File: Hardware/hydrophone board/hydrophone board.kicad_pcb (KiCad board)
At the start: 2 copper layers, 6 parts, among them U1 AD8541ARTZ, U2 AD8648ARZ, U3 XLV320ADC5140IRTWR, U4 DEV-16771, U5 LT1963AxST-3.3, X1 ASE-xxxMHz

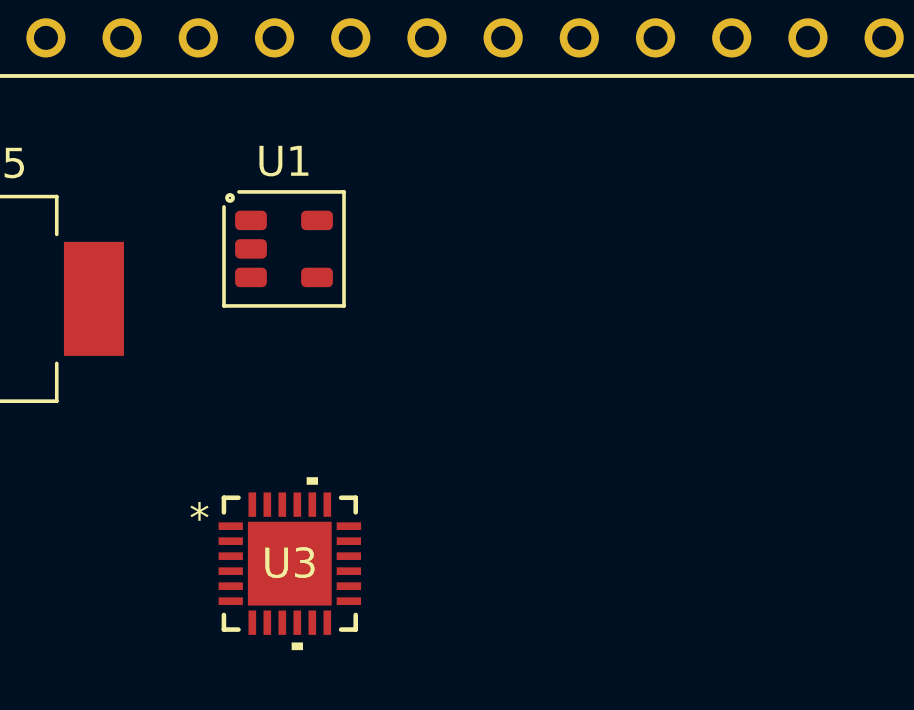
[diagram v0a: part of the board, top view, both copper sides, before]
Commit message: added teensy 3d model
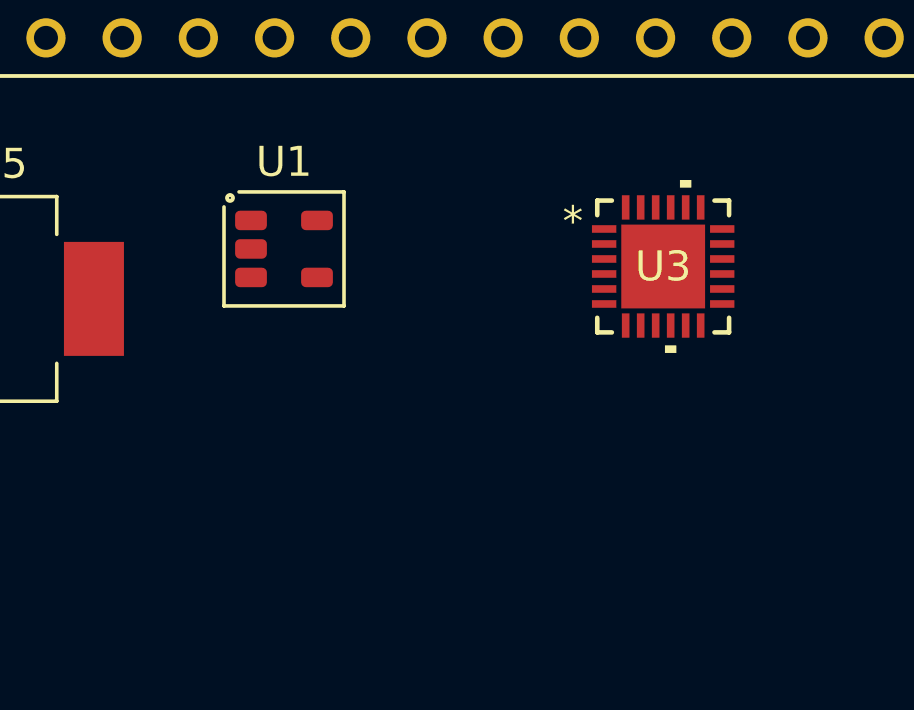
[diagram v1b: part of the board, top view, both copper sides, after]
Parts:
- moved U3 15.9 mm to (149.4, 80.5)
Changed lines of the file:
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@@
   (net 95 "Net-(X1-OUT)")
   (footprint "TLV320ADC5140:RTW24_4P15X4P15_TEX" (layer "F.Cu")
-    (at 136.906 90.424)
+    (at 149.352 80.518)
     (tags "XLV320ADC5140IRTWR ")
     (property "Sheetfile" "adc.kicad_sch")
@@
     (pad "VUSB" thru_hole circle (at -26.67 -5.08) (size 1.308 1.308) (drill 0.8) (layers "*.Cu" "*.Mask")
       (net 41 "unconnected-(U4-PadVUSB)") (pinfunction "VUSB") (pintype "passive") (solder_mask_margin 0.102))
+    (model "${KIPRJMOD}/library/teensy 4.1/footprints.pretty/DEV-16771.step"
+      (offset (xyz 0 0 0))
+      (scale (xyz 1 1 1))
+      (rotate (xyz -90 0 0))
+    )
   )
   (footprint "Package_SO_AKL:SOIC-14_3.9x8.7mm_P1.27mm" (layer "F.Cu")

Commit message: started layout
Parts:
- removed U4: DEV-16771, DEV-16771:MODULE_DEV-16771
- removed X1: ASE-xxxMHz, Oscillator:Oscillator_SMD_Abracon_ASE-4Pin_3.2x2.5mm
- added C111: 0.1u, Capacitor_SMD:C_0603_1608Metric, F.Cu at (101.6, 56.7)
- added C112: 820p, Capacitor_SMD:C_0603_1608Metric, F.Cu at (101.6, 59.2)
- added C113: 6.8u, Capacitor_SMD:C_0805_2012Metric, F.Cu at (105.8, 61.6)
- added C114: 1u, Capacitor_SMD:C_0603_1608Metric, F.Cu at (101.6, 61.7)
- added C121: 0.1u, Capacitor_SMD:C_0603_1608Metric, F.Cu at (103.1, 49.3)
- added C122: 820p, Capacitor_SMD:C_0603_1608Metric, F.Cu at (108.7, 44.7)
- added C123: 6.8u, Capacitor_SMD:C_0805_2012Metric, F.Cu at (100.3, 44.7)
- added C124: 1u, Capacitor_SMD:C_0603_1608Metric, F.Cu at (109.7, 49.3)
- added C131: 0.1u, Capacitor_SMD:C_0603_1608Metric, F.Cu at (152.0, 35.9)
- added C132: 820p, Capacitor_SMD:C_0603_1608Metric, F.Cu at (152.0, 38.4)
- added C133: 6.8u, Capacitor_SMD:C_0805_2012Metric, F.Cu at (156.2, 45.7)
- added C134: 1u, Capacitor_SMD:C_0603_1608Metric, F.Cu at (152.0, 40.9)
- added C141: 0.1u, Capacitor_SMD:C_0603_1608Metric, F.Cu at (140.9, 35.9)
- added C142: 820p, Capacitor_SMD:C_0603_1608Metric, F.Cu at (140.9, 38.4)
- added C143: 6.8u, Capacitor_SMD:C_0805_2012Metric, F.Cu at (145.1, 45.7)
- added C144: 1u, Capacitor_SMD:C_0603_1608Metric, F.Cu at (140.9, 40.9)
- added C211: 360p, Capacitor_SMD:C_0603_1608Metric, F.Cu at (149.8, 77.7)
- added C212: 360p, Capacitor_SMD:C_0603_1608Metric, F.Cu at (149.8, 80.2)
- added C213: 0.1u, Capacitor_SMD:C_0603_1608Metric, F.Cu at (149.8, 82.7)
- added C214: 360p, Capacitor_SMD:C_0603_1608Metric, F.Cu at (149.8, 85.2)
- added C215: 36p, Capacitor_SMD:C_0603_1608Metric, F.Cu at (149.8, 87.7)
- added C216: 36p, Capacitor_SMD:C_0603_1608Metric, F.Cu at (149.8, 90.2)
- added C217: 18p, Capacitor_SMD:C_0603_1608Metric, F.Cu at (153.8, 77.7)
- added C218: 360p, Capacitor_SMD:C_0603_1608Metric, F.Cu at (153.8, 80.2)
- added C221: 360p, Capacitor_SMD:C_0603_1608Metric, F.Cu at (75.7, 108.5)
- added C222: 360p, Capacitor_SMD:C_0603_1608Metric, F.Cu at (75.7, 111.0)
- added C223: 0.1u, Capacitor_SMD:C_0603_1608Metric, F.Cu at (75.7, 113.5)
- added C224: 360p, Capacitor_SMD:C_0603_1608Metric, F.Cu at (75.7, 116.0)
- added C225: 36p, Capacitor_SMD:C_0603_1608Metric, F.Cu at (75.7, 118.6)
- added C226: 36p, Capacitor_SMD:C_0603_1608Metric, F.Cu at (75.7, 121.1)
- added C227: 18p, Capacitor_SMD:C_0603_1608Metric, F.Cu at (79.7, 108.5)
- added C228: 360p, Capacitor_SMD:C_0603_1608Metric, F.Cu at (79.7, 111.0)
- added C231: 360p, Capacitor_SMD:C_0603_1608Metric, F.Cu at (98.4, 108.5)
- added C232: 360p, Capacitor_SMD:C_0603_1608Metric, F.Cu at (98.4, 111.0)
- added C233: 0.1u, Capacitor_SMD:C_0603_1608Metric, F.Cu at (98.4, 113.5)
- added C234: 360p, Capacitor_SMD:C_0603_1608Metric, F.Cu at (98.4, 116.0)
- added C235: 36p, Capacitor_SMD:C_0603_1608Metric, F.Cu at (98.4, 118.6)
- added C236: 36p, Capacitor_SMD:C_0603_1608Metric, F.Cu at (98.4, 121.1)
- added C237: 18p, Capacitor_SMD:C_0603_1608Metric, F.Cu at (102.4, 108.5)
- added C238: 360p, Capacitor_SMD:C_0603_1608Metric, F.Cu at (102.4, 111.0)
- added C241: 360p, Capacitor_SMD:C_0603_1608Metric, F.Cu at (126.7, 102.1)
- added C242: 360p, Capacitor_SMD:C_0603_1608Metric, F.Cu at (126.7, 104.6)
- added C243: 0.1u, Capacitor_SMD:C_0603_1608Metric, F.Cu at (126.7, 107.1)
- added C244: 360p, Capacitor_SMD:C_0603_1608Metric, F.Cu at (126.7, 109.6)
- added C245: 36p, Capacitor_SMD:C_0603_1608Metric, F.Cu at (126.7, 112.1)
- added C246: 36p, Capacitor_SMD:C_0603_1608Metric, F.Cu at (126.7, 114.6)
- added C247: 18p, Capacitor_SMD:C_0603_1608Metric, F.Cu at (130.7, 102.1)
- added C248: 360p, Capacitor_SMD:C_0603_1608Metric, F.Cu at (130.7, 104.6)
- added C301: 0.1u, Capacitor_SMD:C_0603_1608Metric, F.Cu at (131.3, 77.7)
- added C302: 1u, Capacitor_SMD:C_0603_1608Metric, F.Cu at (131.3, 80.2)
- added C303: 0.1u, Capacitor_SMD:C_0603_1608Metric, F.Cu at (131.3, 82.7)
- added C304: 10u, Capacitor_SMD:C_0805_2012Metric, F.Cu at (143.5, 77.9)
- added C305: 1u, Capacitor_SMD:C_0603_1608Metric, F.Cu at (131.3, 85.2)
- added C306: 0.1u, Capacitor_SMD:C_0603_1608Metric, F.Cu at (131.3, 87.7)
- added C307: 10u, Capacitor_SMD:C_0805_2012Metric, F.Cu at (143.5, 80.9)
- added C308: 1u, Capacitor_SMD:C_0603_1608Metric, F.Cu at (131.3, 90.2)
- added C309: 0.1u, Capacitor_SMD:C_0603_1608Metric, F.Cu at (131.3, 92.7)
- added C310: 1u, Capacitor_SMD:C_0603_1608Metric, F.Cu at (135.3, 77.7)
- added C311: 1u, Capacitor_SMD:C_0603_1608Metric, F.Cu at (135.3, 80.2)
- added C312: 1u, Capacitor_SMD:C_0603_1608Metric, F.Cu at (135.3, 82.7)
- added C313: 1u, Capacitor_SMD:C_0603_1608Metric, F.Cu at (135.3, 85.2)
- added C314: 1u, Capacitor_SMD:C_0603_1608Metric, F.Cu at (135.3, 87.7)
- added C315: 1u, Capacitor_SMD:C_0603_1608Metric, F.Cu at (135.3, 90.2)
- added C316: 1u, Capacitor_SMD:C_0603_1608Metric, F.Cu at (135.3, 92.7)
- added C317: 1u, Capacitor_SMD:C_0603_1608Metric, F.Cu at (139.3, 77.7)
- added C318: 1u, Capacitor_SMD:C_0603_1608Metric, F.Cu at (139.3, 80.2)
- added C501: 1u, Capacitor_SMD:C_0603_1608Metric, F.Cu at (154.1, 102.1)
- added C502: 22u, Capacitor_SMD:C_0805_2012Metric, F.Cu at (162.9, 102.3)
- added C503: 22u, Capacitor_SMD:C_0805_2012Metric, F.Cu at (162.9, 105.3)
- added C504: 1u, Capacitor_SMD:C_0603_1608Metric, F.Cu at (154.1, 104.6)
- added C505: 22u, Capacitor_SMD:C_0805_2012Metric, F.Cu at (162.9, 108.3)
- added C506: 1u, Capacitor_SMD:C_0603_1608Metric, F.Cu at (154.1, 107.1)
- added D501: LED, LED_SMD:LED_0805_2012Metric, F.Cu at (158.3, 112.0)
- added D502: LED, LED_SMD:LED_0805_2012Metric, F.Cu at (158.3, 115.1)
- added J1: AudioJack3_Ground, Connector_Audio:Jack_3.5mm_CUI_SJ-3524-SMT_Horizontal, F.Cu at (72.4, 44.5)
- added J2: AudioJack3_Ground, Connector_Audio:Jack_3.5mm_CUI_SJ-3524-SMT_Horizontal, F.Cu at (72.4, 59.7)
- added J3: AudioJack3_Ground, Connector_Audio:Jack_3.5mm_CUI_SJ-3524-SMT_Horizontal, F.Cu at (72.4, 73.7)
- added J301: Conn_01x08, Connector_PinSocket_2.54mm:PinSocket_1x08_P2.54mm_Vertical, F.Cu at (127.0, 78.7)
- added J4: AudioJack3_Ground, Connector_Audio:Jack_3.5mm_CUI_SJ-3524-SMT_Horizontal, F.Cu at (72.4, 88.9)
- added J401: Conn_01x07, Connector_PinHeader_2.54mm:PinHeader_1x07_P2.54mm_Vertical, F.Cu at (219.7, 50.8)
- added J5: Conn_01x02, Connector_PinHeader_2.54mm:PinHeader_1x02_P2.54mm_Vertical, F.Cu at (76.0, 100.4)
- added J501: Conn_01x03, Connector_PinSocket_2.54mm:PinSocket_1x03_P2.54mm_Vertical, F.Cu at (158.4, 103.1)
- added J6: Conn_01x02, Connector_PinHeader_2.54mm:PinHeader_1x02_P2.54mm_Vertical, F.Cu at (80.7, 100.4)
- added J7: Conn_01x02, Connector_PinHeader_2.54mm:PinHeader_1x02_P2.54mm_Vertical, F.Cu at (85.3, 100.4)
- added J8: Conn_01x02, Connector_PinHeader_2.54mm:PinHeader_1x02_P2.54mm_Vertical, F.Cu at (90.0, 100.4)
- added L501: L_Ferrite_Small, Inductor_SMD:L_0805_2012Metric, F.Cu at (162.8, 111.9)
- added R111: 715, Resistor_SMD:R_0603_1608Metric, F.Cu at (101.6, 64.2)
- added R112: 360, Resistor_SMD:R_0603_1608Metric, F.Cu at (101.6, 66.7)
- added R113: 10k, Resistor_SMD:R_0603_1608Metric, F.Cu at (101.6, 69.3)
- added R114: 10k, Resistor_SMD:R_0603_1608Metric, F.Cu at (101.6, 71.8)
- added R121: 715, Resistor_SMD:R_0603_1608Metric, F.Cu at (111.3, 44.7)
- added R122: 360, Resistor_SMD:R_0603_1608Metric, F.Cu at (100.3, 49.3)
- added R123: 10k, Resistor_SMD:R_0603_1608Metric, F.Cu at (106.4, 48.5)
- added R124: 10k, Resistor_SMD:R_0603_1608Metric, F.Cu at (112.3, 49.3)
- added R131: 715, Resistor_SMD:R_0603_1608Metric, F.Cu at (152.0, 43.4)
- added R132: 360, Resistor_SMD:R_0603_1608Metric, F.Cu at (152.0, 46.0)
- added R133: 10k, Resistor_SMD:R_0603_1608Metric, F.Cu at (152.0, 48.5)
- added R134: 10k, Resistor_SMD:R_0603_1608Metric, F.Cu at (152.0, 51.0)
- added R141: 715, Resistor_SMD:R_0603_1608Metric, F.Cu at (140.9, 43.4)
- added R142: 360, Resistor_SMD:R_0603_1608Metric, F.Cu at (140.9, 46.0)
- added R143: 10k, Resistor_SMD:R_0603_1608Metric, F.Cu at (140.9, 48.5)
- added R144: 10k, Resistor_SMD:R_0603_1608Metric, F.Cu at (140.9, 51.0)
- added R211: 5.62k, Resistor_SMD:R_0603_1608Metric, F.Cu at (153.8, 82.7)
- added R212: 169k, Resistor_SMD:R_0603_1608Metric, F.Cu at (153.8, 85.2)
- added R213: 8.45k, Resistor_SMD:R_0603_1608Metric, F.Cu at (153.8, 87.7)
- added R214: 115k, Resistor_SMD:R_0603_1608Metric, F.Cu at (153.8, 90.2)
- added R215: 44.2k, Resistor_SMD:R_0603_1608Metric, F.Cu at (157.8, 77.7)
- added R216: 44.2k, Resistor_SMD:R_0603_1608Metric, F.Cu at (157.8, 80.2)
- added R217: 9.76k, Resistor_SMD:R_0603_1608Metric, F.Cu at (157.8, 82.7)
- added R221: 5.62k, Resistor_SMD:R_0603_1608Metric, F.Cu at (79.7, 113.5)
- added R222: 169k, Resistor_SMD:R_0603_1608Metric, F.Cu at (79.7, 116.0)
- added R223: 8.45k, Resistor_SMD:R_0603_1608Metric, F.Cu at (79.7, 118.6)
- added R224: 115k, Resistor_SMD:R_0603_1608Metric, F.Cu at (79.7, 121.1)
- added R225: 44.2k, Resistor_SMD:R_0603_1608Metric, F.Cu at (83.7, 108.5)
- added R226: 44.2k, Resistor_SMD:R_0603_1608Metric, F.Cu at (83.7, 111.0)
- added R227: 9.76k, Resistor_SMD:R_0603_1608Metric, F.Cu at (83.7, 113.5)
- added R231: 5.62k, Resistor_SMD:R_0603_1608Metric, F.Cu at (102.4, 113.5)
- added R232: 169k, Resistor_SMD:R_0603_1608Metric, F.Cu at (102.4, 116.0)
- added R233: 8.45k, Resistor_SMD:R_0603_1608Metric, F.Cu at (102.4, 118.6)
- added R234: 115k, Resistor_SMD:R_0603_1608Metric, F.Cu at (102.4, 121.1)
- added R235: 44.2k, Resistor_SMD:R_0603_1608Metric, F.Cu at (106.5, 108.5)
- added R236: 44.2k, Resistor_SMD:R_0603_1608Metric, F.Cu at (106.5, 111.0)
- added R237: 9.76k, Resistor_SMD:R_0603_1608Metric, F.Cu at (106.5, 113.5)
- added R241: 5.62k, Resistor_SMD:R_0603_1608Metric, F.Cu at (130.7, 107.1)
- added R242: 169k, Resistor_SMD:R_0603_1608Metric, F.Cu at (130.7, 109.6)
- added R243: 8.45k, Resistor_SMD:R_0603_1608Metric, F.Cu at (130.7, 112.1)
- added R244: 115k, Resistor_SMD:R_0603_1608Metric, F.Cu at (130.7, 114.6)
- added R245: 44.2k, Resistor_SMD:R_0603_1608Metric, F.Cu at (134.7, 102.1)
- added R246: 44.2k, Resistor_SMD:R_0603_1608Metric, F.Cu at (134.7, 104.6)
- added R247: 9.76k, Resistor_SMD:R_0603_1608Metric, F.Cu at (134.7, 107.1)
- added R301: 2k, Resistor_SMD:R_0603_1608Metric, F.Cu at (139.3, 82.7)
- added R302: 2k, Resistor_SMD:R_0603_1608Metric, F.Cu at (139.3, 85.2)
- added R303: 1k, Resistor_SMD:R_0603_1608Metric, F.Cu at (139.3, 87.7)
- added R304: 1k, Resistor_SMD:R_0603_1608Metric, F.Cu at (139.3, 90.2)
- added R305: 1k, Resistor_SMD:R_0603_1608Metric, F.Cu at (139.3, 92.7)
- added R501: 470, Resistor_SMD:R_0603_1608Metric, F.Cu at (154.1, 109.6)
- added R502: 470, Resistor_SMD:R_0603_1608Metric, F.Cu at (154.1, 112.1)
- added TP111: TestPoint_Probe, Connector_PinHeader_2.54mm:PinHeader_1x01_P2.54mm_Vertical, F.Cu at (105.9, 57.8)
- added TP121: TestPoint_Probe, Connector_PinHeader_2.54mm:PinHeader_1x01_P2.54mm_Vertical, F.Cu at (118.1, 44.5)
- added TP131: TestPoint_Probe, Connector_PinHeader_2.54mm:PinHeader_1x01_P2.54mm_Vertical, F.Cu at (156.3, 41.9)
- added TP141: TestPoint_Probe, Connector_PinHeader_2.54mm:PinHeader_1x01_P2.54mm_Vertical, F.Cu at (145.2, 41.9)
- added TP211: TestPoint_Probe, Connector_PinHeader_2.54mm:PinHeader_1x01_P2.54mm_Vertical, F.Cu at (162.1, 78.7)
- added TP221: TestPoint_Probe, Connector_PinHeader_2.54mm:PinHeader_1x01_P2.54mm_Vertical, F.Cu at (88.0, 119.9)
- added TP231: TestPoint_Probe, Connector_PinHeader_2.54mm:PinHeader_1x01_P2.54mm_Vertical, F.Cu at (110.8, 119.9)
- added TP241: TestPoint_Probe, Connector_PinHeader_2.54mm:PinHeader_1x01_P2.54mm_Vertical, F.Cu at (139.0, 113.5)
- added TP501: TestPoint_Probe, Connector_PinHeader_2.54mm:PinHeader_1x01_P2.54mm_Vertical, F.Cu at (149.8, 103.1)
- added TP502: TestPoint_Probe, Connector_PinHeader_2.54mm:PinHeader_1x01_P2.54mm_Vertical, F.Cu at (149.8, 107.8)
- added TP503: TestPoint_Probe, Connector_PinHeader_2.54mm:PinHeader_1x01_P2.54mm_Vertical, F.Cu at (149.8, 112.4)
- added TP504: TestPoint_Probe, Connector_PinHeader_2.54mm:PinHeader_1x01_P2.54mm_Vertical, F.Cu at (149.8, 117.1)
- added U121: AD8541ARTZ, Package_TO_SOT_SMD_AKL:SOT-23-5, F.Cu at (104.6, 44.7)
- added U131: AD8541ARTZ, Package_TO_SOT_SMD_AKL:SOT-23-5, F.Cu at (156.6, 37.1)
- added U141: AD8541ARTZ, Package_TO_SOT_SMD_AKL:SOT-23-5, F.Cu at (145.5, 37.1)
- added U221: AD8648ARZ, Package_SO_AKL:SOIC-14_3.9x8.7mm_P1.27mm, F.Cu at (90.1, 112.4)
- added U231: AD8648ARZ, Package_SO_AKL:SOIC-14_3.9x8.7mm_P1.27mm, F.Cu at (112.8, 112.4)
- added U241: AD8648ARZ, Package_SO_AKL:SOIC-14_3.9x8.7mm_P1.27mm, F.Cu at (141.1, 106.0)
- added U401: DEV-16771, DEV-16771:MODULE_DEV-16771, F.Cu at (203.2, 68.6)
- moved U211 82.1 mm to (190.1, 117.8)
- moved U301 82.1 mm to (223.5, 115.7)
- moved U501 82.1 mm to (201.4, 116.8)
- moved U111 33.1 mm to (106.4, 66.5)
- renumbered U1 to U111, U2 to U211, U3 to U301, U5 to U501
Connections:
- net /adc/IN_1_B renamed /IN_1_B
- U111 pad 1: /low pass filter/IN -> /IN_1_A
- U301 pad 13: unconnected-(U3-IN4M_GPO4-Pad13) -> /adc/IN4M
- U301 pad 20: /adc/MCLK -> /adc/SDOUT_2
- U501 pad 3: +3.3VA -> Net-(J501-Pin_1)
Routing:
- net Net-(U121-+): track 0.00 -> 12.7 mm
- net Net-(U121--): track 0.00 -> 11.2 mm
- net GND: track 0.00 -> 7.48 mm, vias 0 -> 3
- net /IN_2_A: track 0.00 -> 5.34 mm
- net +3.3VA: track 0.00 -> 5.25 mm
- net /IN_2: track 0.00 -> 2.54 mm

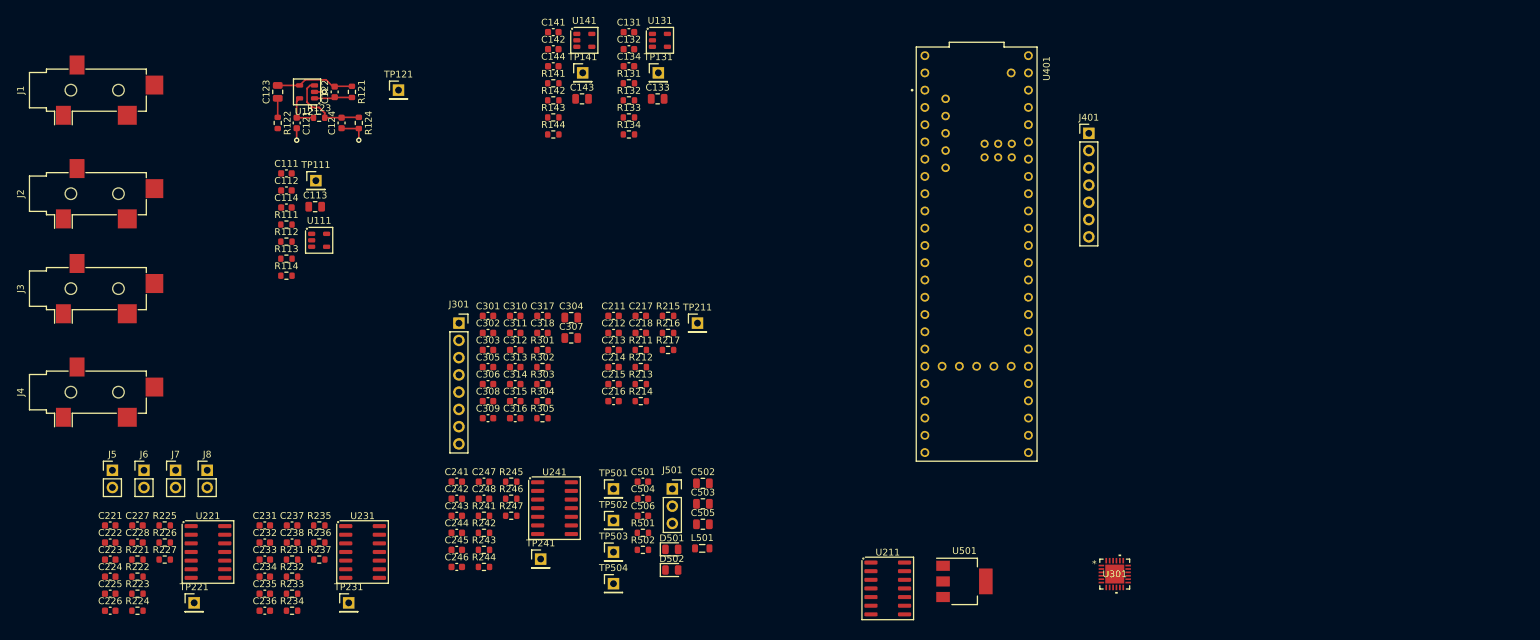
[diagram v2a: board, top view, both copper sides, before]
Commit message: changed all cap + resistors to 0805, starting filter layout
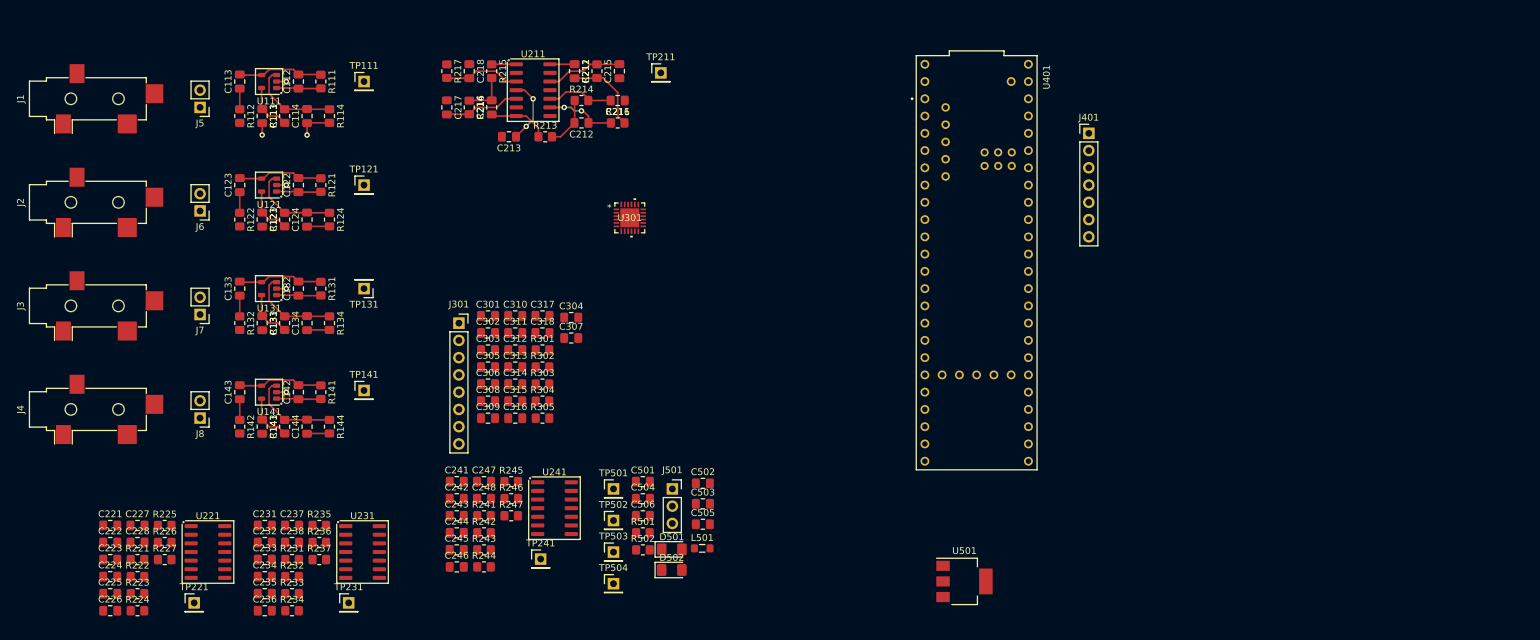
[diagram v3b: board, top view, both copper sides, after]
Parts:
- C111, C112, C114, C121, C122, C124, C131, C132, C134, C141, C142, C144, C211, C212, C213, C214, C215, C216, C217, C218, C221, C222, C223, C224, C225, C226, C227, C228, C231, C232, C233, C234, C235, C236, C237, C238, C241, C242, C243, C244, C245, C246, C247, C248, C301, C302, C303, C305, C306, C308, C309, C310, C311, C312, C313, C314, C315, C316, C317, C318, C501, C504, C506: footprint Capacitor_SMD:C_0603_1608Metric -> Capacitor_SMD:C_0805_2012Metric_Pad1.18x1.45mm_HandSolder
- C113, C123, C133, C143, C304, C307, C502, C503, C505: footprint Capacitor_SMD:C_0805_2012Metric -> Capacitor_SMD:C_0805_2012Metric_Pad1.18x1.45mm_HandSolder
- D501, D502: footprint LED_SMD:LED_0805_2012Metric -> LED_SMD:LED_1206_3216Metric_Pad1.42x1.75mm_HandSolder
- L501: footprint Inductor_SMD:L_0805_2012Metric -> Inductor_SMD:L_0805_2012Metric_Pad1.05x1.20mm_HandSolder
- R111, R112, R113, R114, R121, R122, R123, R124, R131, R132, R133, R134, R141, R142, R143, R144, R211, R212, R213, R214, R215, R216, R217, R221, R222, R223, R224, R225, R226, R227, R231, R232, R233, R234, R235, R236, R237, R241, R242, R243, R244, R245, R246, R247, R301, R302, R303, R304, R305, R501, R502: footprint Resistor_SMD:R_0603_1608Metric -> Resistor_SMD:R_0805_2012Metric_Pad1.20x1.40mm_HandSolder
- moved U211 90.0 mm to (137.9, 44.5)
- moved U301 88.6 mm to (152.1, 63.2)
- moved C141 72.2 mm to (98.0, 94.0), turned to -90 degrees
- moved U141 69.5 mm to (99.1, 88.9), turned to 180 degrees
- moved C131 68.9 mm to (98.0, 78.7), turned to -90 degrees
- moved U131 68.2 mm to (99.1, 73.7), turned to 180 degrees
- moved C133 67.6 mm to (94.7, 73.7), turned to 90 degrees
- moved R142 66.6 mm to (94.7, 94.0), turned to -90 degrees
- moved C143 66.3 mm to (94.7, 88.9), turned to 90 degrees
- moved R132 66.0 mm to (94.7, 78.7), turned to -90 degrees
- moved C144 64.2 mm to (104.6, 94.0), turned to 90 degrees
- moved C142 62.9 mm to (103.4, 88.9), turned to 90 degrees
- moved C134 60.6 mm to (104.6, 78.7), turned to 90 degrees
- moved R143 60.3 mm to (101.3, 94.0), turned to 90 degrees
- moved C132 60.1 mm to (103.4, 73.7), turned to 90 degrees
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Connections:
- J5 pad 1: /IN_1 -> GND
- J5 pad 2: GND -> /IN_1
- J6 pad 1: /IN_2 -> GND
- J6 pad 2: GND -> /IN_2
- J7 pad 1: /IN_3 -> GND
- J7 pad 2: GND -> /IN_3
- J8 pad 1: /IN_4 -> GND
- J8 pad 2: GND -> /IN_4
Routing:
- net +3.3VA: track 5.25 -> 38.7 mm, vias 0 -> 2
- net GND: track 7.48 -> 22.5 mm, vias 3 -> 6
- net Net-(U141-+): track 0.00 -> 13.4 mm
- net Net-(U111-+): track 0.00 -> 13.4 mm
- net Net-(U131-+): track 0.00 -> 13.4 mm
- net Net-(U141--): track 0.00 -> 12.6 mm
- net Net-(U111--): track 0.00 -> 12.6 mm
- net Net-(U131--): track 0.00 -> 12.6 mm
- net Net-(C211-Pad2): track 0.00 -> 12.1 mm
- net Net-(U211A-+): track 0.00 -> 11.3 mm
- net Net-(U211D-+): track 0.00 -> 11.3 mm
- net Net-(U211B-+): track 0.00 -> 11.2 mm
- net Net-(U211C--): track 0.00 -> 10.5 mm, vias 0 -> 2
- net Net-(U211C-+): track 0.00 -> 10.0 mm
- net Net-(U211B--): track 0.00 -> 8.97 mm
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
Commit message: Update hydrophone board.kicad_pcb
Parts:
- J301: footprint Connector_PinSocket_2.54mm:PinSocket_1x08_P2.54mm_Vertical -> Connector_PinHeader_2.54mm:PinHeader_1x08_P2.54mm_Vertical
- J501: footprint Connector_PinSocket_2.54mm:PinSocket_1x03_P2.54mm_Vertical -> Connector_PinHeader_2.54mm:PinHeader_1x03_P2.54mm_Vertical
- moved J301 155.0 mm to (282.0, 79.8)
- moved C225 91.6 mm to (144.8, 58.4), turned to 90 degrees
- moved C226 90.4 mm to (144.5, 62.5), turned to 180 degrees
- moved TP221 88.1 mm to (151.1, 58.4)
- moved R222 84.5 mm to (141.5, 58.4), turned to 90 degrees
- moved R224 83.5 mm to (139.2, 62.5)
- moved R221 80.5 mm to (144.5, 65.8)
- moved C221 80.1 mm to (138.2, 58.4), turned to -90 degrees
- moved C222 78.0 mm to (139.2, 65.8), turned to 180 degrees
- moved R223 74.2 mm to (133.9, 67.8)
- moved C224 72.7 mm to (126.0, 63.5), turned to 90 degrees
- moved C223 69.9 mm to (128.5, 67.8), turned to 180 degrees
- moved C228 67.9 mm to (122.7, 58.4), turned to -90 degrees
- moved U221 66.4 mm to (132.1, 61.0)
- moved R227 65.7 mm to (119.4, 58.4), turned to -90 degrees
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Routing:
- net GND: track 22.5 -> 150.7 mm, vias 6 -> 43
- net +3.3VA: track 38.7 -> 96.0 mm, vias 2 -> 8
- net /IN_4: track 3.04 -> 32.2 mm
- net /IN_3: track 3.04 -> 32.2 mm
- net /IN_1: track 3.04 -> 32.2 mm
- net /IN_2: track 3.04 -> 32.2 mm
- net +3.3VD: track 0.00 -> 28.2 mm, vias 0 -> 2
- net Net-(U231C--): track 0.00 -> 14.9 mm, vias 0 -> 2
- net Net-(U241C--): track 0.00 -> 14.9 mm, vias 0 -> 2
- net Net-(U221C--): track 0.00 -> 14.9 mm, vias 0 -> 2
- net Net-(U301-VREF): track 0.00 -> 14.7 mm
- net /IN_4_A: track 6.57 -> 20.2 mm
- net /IN_2_A: track 6.57 -> 20.2 mm
- net /IN_1_A: track 6.57 -> 20.2 mm
- net /IN_3_A: track 6.52 -> 20.2 mm
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
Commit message: changed some aprts
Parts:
- removed J301: Conn_01x08, Connector_PinHeader_2.54mm:PinHeader_1x08_P2.54mm_Vertical
- removed J501: Conn_01x03, Connector_PinHeader_2.54mm:PinHeader_1x03_P2.54mm_Vertical
- removed TP111, TP121, TP131, TP141, TP211, TP221, TP231, TP241: TestPoint_Probe, Connector_PinHeader_2.54mm:PinHeader_1x01_P2.54mm_Vertical
- added J111: Conn_01x02, Connector_PinHeader_2.54mm:PinHeader_1x02_P2.54mm_Vertical, F.Cu at (124.4, 119.4)
- added J121: Conn_01x02, Connector_PinHeader_2.54mm:PinHeader_1x02_P2.54mm_Vertical, F.Cu at (131.1, 119.4)
- added J131: Conn_01x02, Connector_PinHeader_2.54mm:PinHeader_1x02_P2.54mm_Vertical, F.Cu at (131.1, 110.2)
- added J141: Conn_01x02, Connector_PinHeader_2.54mm:PinHeader_1x02_P2.54mm_Vertical, F.Cu at (111.1, 119.4)
- added J211: Conn_01x02, Connector_PinHeader_2.54mm:PinHeader_1x02_P2.54mm_Vertical, F.Cu at (124.4, 110.2)
- added J221: Conn_01x02, Connector_PinHeader_2.54mm:PinHeader_1x02_P2.54mm_Vertical, F.Cu at (117.8, 110.2)
- added J231: Conn_01x02, Connector_PinHeader_2.54mm:PinHeader_1x02_P2.54mm_Vertical, F.Cu at (117.8, 119.4)
- added J241: Conn_01x02, Connector_PinHeader_2.54mm:PinHeader_1x02_P2.54mm_Vertical, F.Cu at (111.1, 110.2)
- added JP501: Jumper_3_Bridged12, PCM_4ms_SolderJumper:JUMPER_SMD_1x3, F.Cu at (167.9, 87.9)
- moved TP501 85.4 mm to (210.8, 43.4)
- moved J401 35.0 mm to (212.3, 78.7), turned to 180 degrees
- moved TP504 29.7 mm to (156.5, 88.1)
- moved R501 28.0 mm to (179.3, 89.2), turned to 180 degrees
- moved TP503 24.5 mm to (152.7, 88.1)
- moved U401 23.0 mm to (195.6, 68.6)
- moved TP502 22.3 mm to (160.3, 88.1)
- moved U501 19.1 mm to (171.7, 94.7)
- moved C505 18.6 mm to (156.0, 97.0)
- moved C501 18.6 mm to (181.1, 97.0)
- moved C502 18.6 mm to (177.8, 97.0)
- moved C503 18.6 mm to (165.9, 97.0)
- moved C504 18.6 mm to (162.6, 97.0)
- moved C506 18.6 mm to (152.7, 97.0)
- moved D501 18.6 mm to (179.3, 92.5)
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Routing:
- net +3.3VD: track 28.2 -> 39.3 mm
- net +3.3VA: track 96.0 -> 103.3 mm
- net GND: track 150.7 -> 156.1 mm, vias 43 -> 47
- net Net-(D501-K): track 6.57 -> 3.50 mm
- net Net-(JP501-A): track 4.70 -> 3.71 mm

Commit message: Update hydrophone board.kicad_pcb
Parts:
- moved TP501 53.8 mm to (175.3, 83.8)
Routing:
- net GND: track 156.1 -> 156.6 mm
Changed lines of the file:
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@@
   )
   (footprint "Connector_PinHeader_2.54mm:PinHeader_1x01_P2.54mm_Vertical" (layer "F.Cu")
-    (at 210.82 43.434)
+    (at 175.26 83.82)
     (descr "Through hole straight pin header, 1x01, 2.54mm pitch, single row")
     (tags "Through hole pin header THT 1x01 2.54mm single row")
@@
   (segment (start 145.5635 62.484) (end 147.066 62.484) (width 0.25) (layer "F.Cu") (net 1))
   (segment (start 104.6855 79.74) (end 104.648 79.7775) (width 0.25) (layer "F.Cu") (net 1))
+  (segment (start 176.276 74.4435) (end 176.2975 74.422) (width 0.5) (layer "F.Cu") (net 1))
   (segment (start 167.132 53.5725) (end 170.18 53.5725) (width 0.5) (layer "F.Cu") (net 1))
   (segment (start 152.654 95.9905) (end 155.956 95.9905) (width 0.5) (layer "F.Cu") (net 1))
@@
   (segment (start 145.5635 77.724) (end 145.5635 75.481) (width 0.25) (layer "F.Cu") (net 1))
   (segment (start 134.555 91.44) (end 136.398 91.44) (width 0.25) (layer "F.Cu") (net 1))
+  (segment (start 176.2975 74.422) (end 178.308 74.422) (width 0.5) (layer "F.Cu") (net 1))
   (segment (start 171.5305 98.0655) (end 171.704 97.892) (width 0.5) (layer "F.Cu") (net 1))
   (segment (start 100.16 88.9) (end 101.6 88.9) (width 0.25) (layer "F.Cu") (net 1))
@@
   (segment (start 145.5635 92.964) (end 145.5635 90.721) (width 0.25) (layer "F.Cu") (net 1))
   (segment (start 107.95 64.5) (end 104.6855 64.5) (width 0.25) (layer "F.Cu") (net 1))
-  (segment (start 173.228 74.4435) (end 173.228 75.946) (width 0.5) (layer "F.Cu") (net 1))
   (segment (start 122.682 57.3825) (end 122.682 55.88) (width 0.25) (layer "F.Cu") (net 1))
   (segment (start 104.648 64.5375) (end 104.648 66.294) (width 0.25) (layer "F.Cu") (net 1))
@@
   (via (at 119.38 60.96) (size 0.8) (drill 0.4) (layers "F.Cu" "B.Cu") (net 1))
   (via (at 147.066 62.484) (size 0.8) (drill 0.4) (layers "F.Cu" "B.Cu") (net 1))
-  (via (at 173.228 75.946) (size 0.8) (drill 0.4) (layers "F.Cu" "B.Cu") (net 1))
+  (via (at 178.308 74.422) (size 0.8) (drill 0.4) (layers "F.Cu" "B.Cu") (net 1))
   (via (at 171.704 94.742) (size 0.8) (drill 0.4) (layers "F.Cu" "B.Cu") (net 1))
   (via (at 147.066 77.724) (size 0.8) (drill 0.4) (layers "F.Cu" "B.Cu") (net 1))
